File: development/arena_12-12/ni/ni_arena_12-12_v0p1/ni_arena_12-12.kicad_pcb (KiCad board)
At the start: 6 copper layers, 228.6 x 228.6 mm, 581 parts, among them J1 Barrel_Jack, J2 NI_TE_68pos, J3 Barrel_Jack, P1 CONN15, P10 CONN15, P11 CONN15, P12 CONN15, P2 CONN15, P3 CONN15, P4 CONN15, P5 CONN15, P6 CONN15, P7 CONN15, P8 CONN15, P9 CONN15, Q1 MOSFET_NCHAN, SW1 SW_SPDT, U1 AP2112K-3.3, U10 TXB0108PW, U100 74LVC2G17, U101 74LVC2G17, U102 74LVC2G17, U103 74LVC2G17, U104 74LVC2G17, U105 74LVC2G17, U106 74LVC2G17, U107 74LVC2G17, U108 74LVC2G17, U109 74LVC2G17, U11 TXB0108PW, U110 74LVC2G17, U12 TXB0108PW, U13 TXB0108PW, U14 TXB0108PW, U15 TXB0108PW, U16 TXB0108PW, U17 TXB0108PW, U18 TXB0108PW, U19 74LVC2G17, U2 TXB0108PW, U20 74LVC2G17, U21 74LVC2G17, U22 74LVC2G17, U23 74LVC2G17, U24 74LVC2G17, U25 74LVC2G17, U26 74LVC2G17, U27 74LVC2G17, U28 74LVC2G17, U29 74LVC2G17, U3 TXB0108PW, U30 74LVC2G17, U31 74LVC2G17, U32 74LVC2G17, U33 74LVC2G17, U34 74LVC2G17, U35 74LVC2G17, U36 74LVC2G17, U37 74LVC2G17, U38 74LVC2G17, U39 74LVC2G17, U4 TXB0108PW, U40 74LVC2G17, U41 74LVC2G17, U42 74LVC2G17, U43 74LVC2G17, U44 74LVC2G17, U45 74LVC2G17, U46 74LVC2G17, U47 74LVC2G17, U48 74LVC2G17, U49 74LVC2G17, U5 TXB0108PW, U50 74LVC2G17, U51 74LVC2G17, U52 74LVC2G17, U53 74LVC2G17, U54 74LVC2G17, U55 74LVC2G17, U56 74LVC2G17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

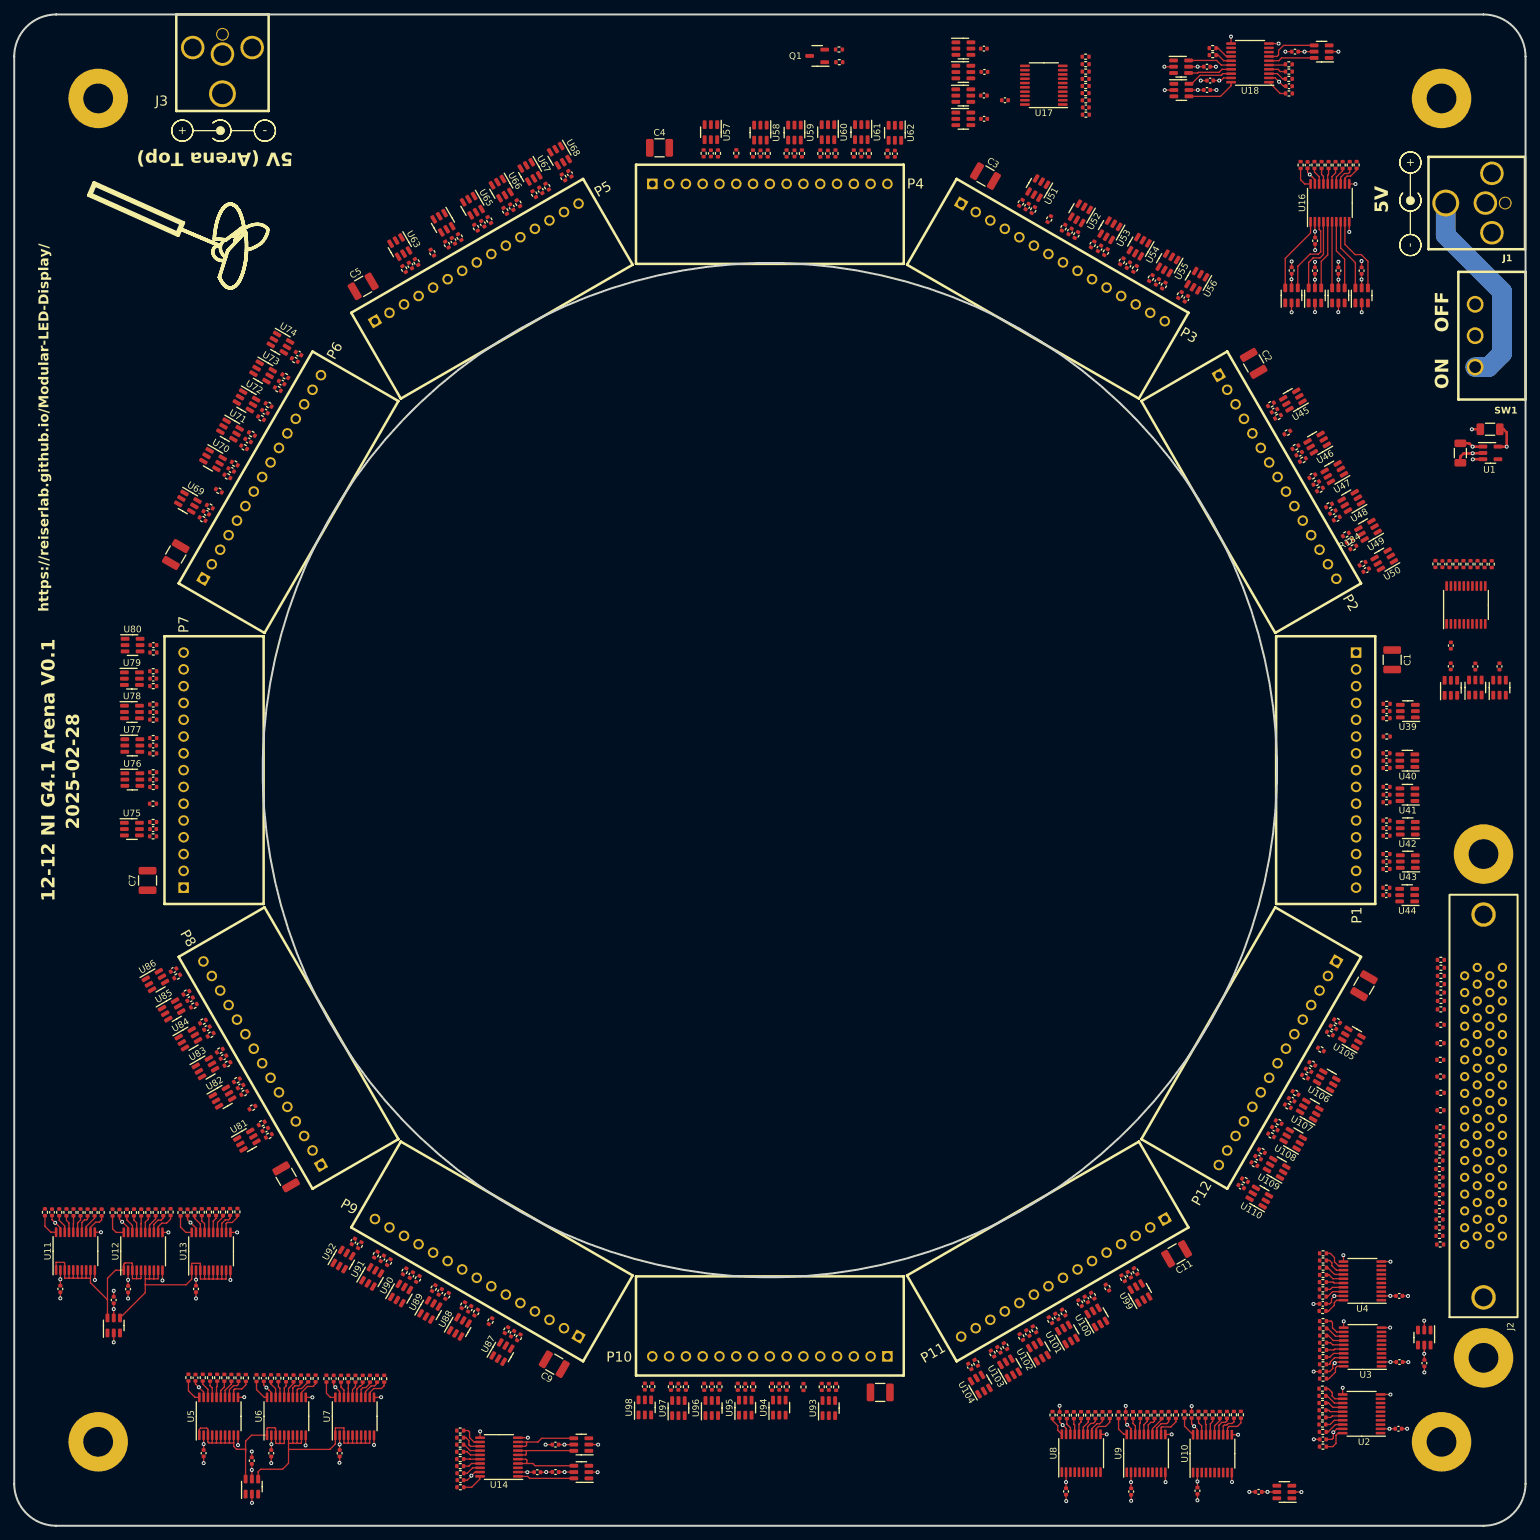
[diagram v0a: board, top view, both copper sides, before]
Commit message: Worked on routing 12-12 NI arena.
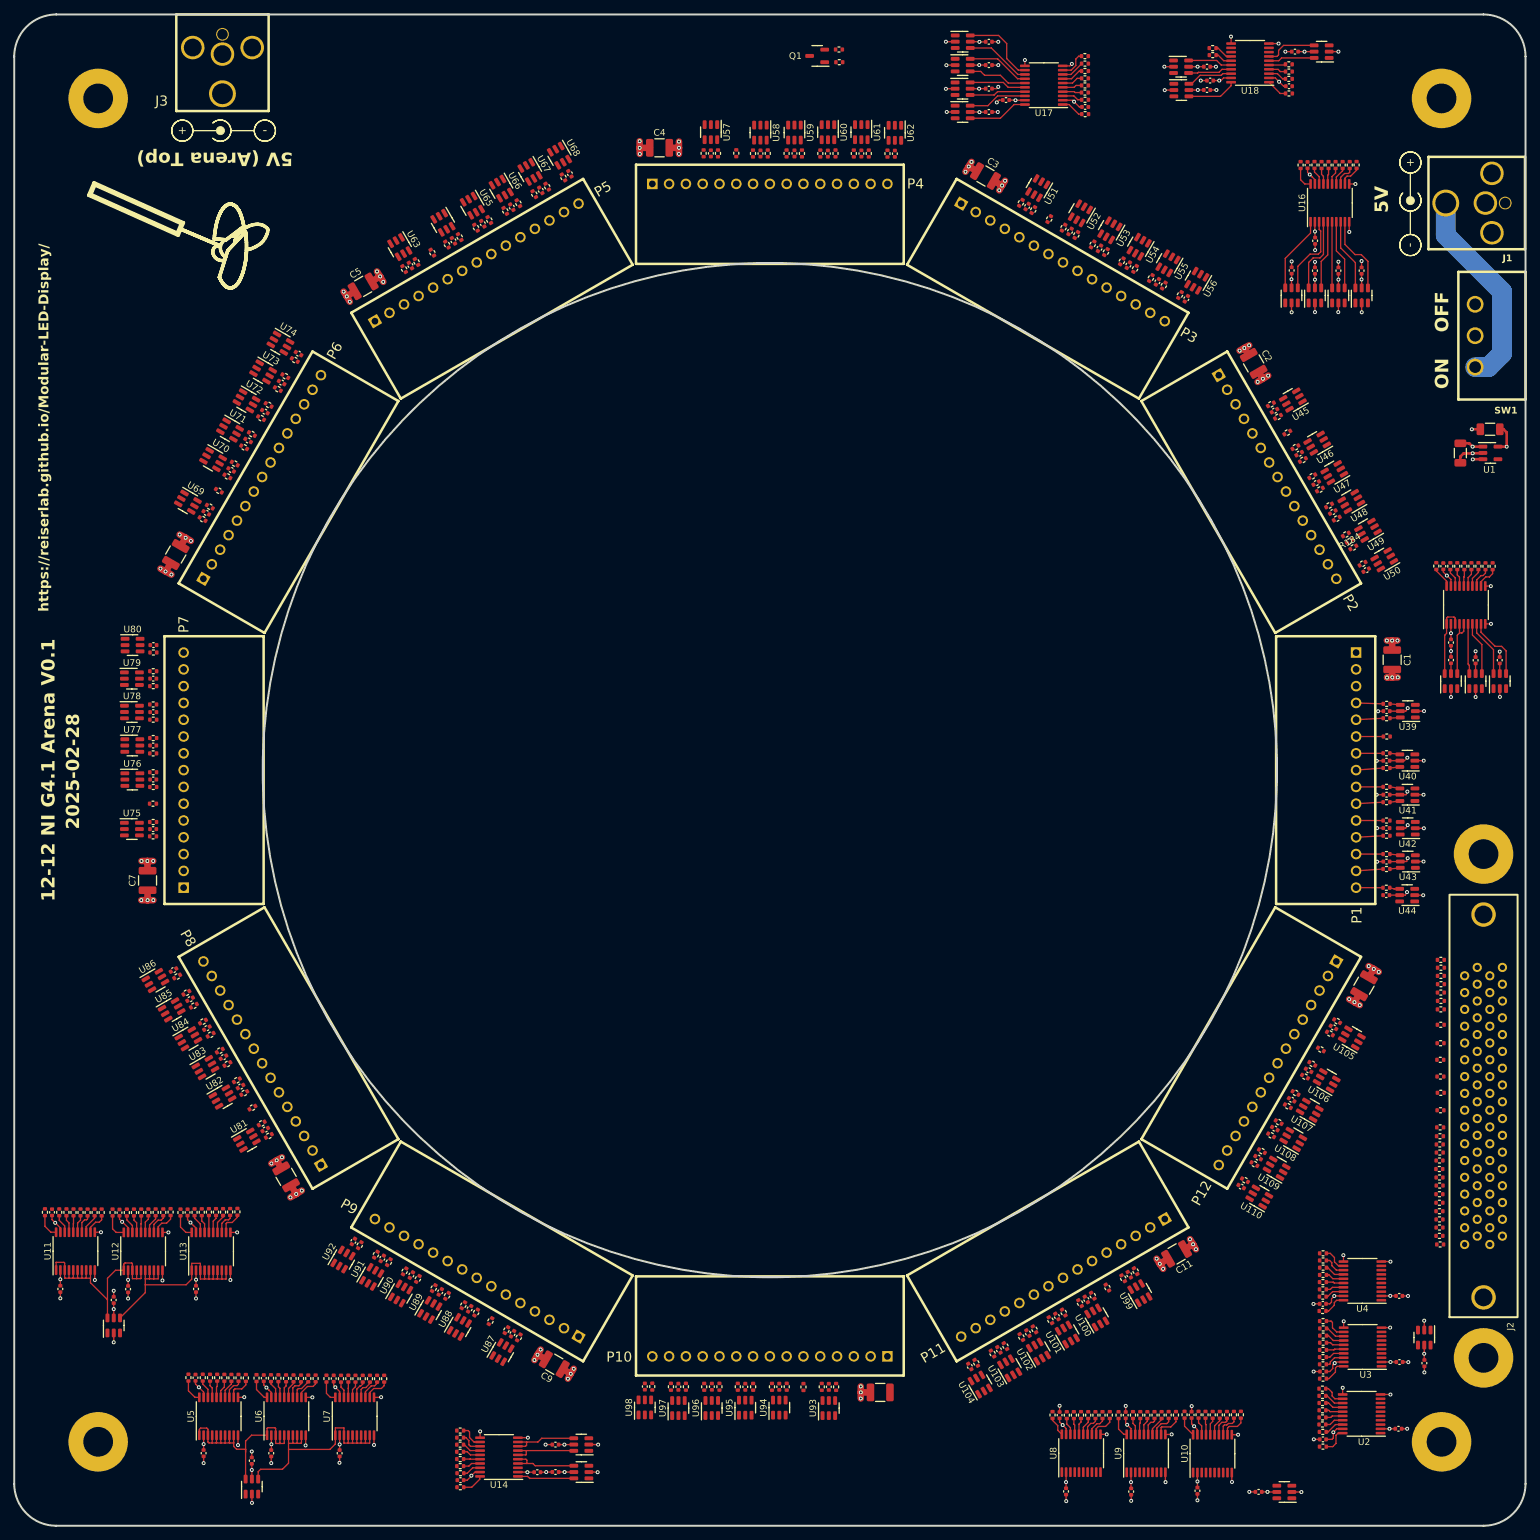
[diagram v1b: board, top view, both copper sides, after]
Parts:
- moved C30 1.28 mm to (210.9, 74.7)
- moved C31 1.28 mm to (210.9, 67.6)
- moved C28 1.26 mm to (210.9, 78.2)
- moved C29 1.23 mm to (210.9, 71.2)
- moved U30 1.06 mm to (207.0, 71.2)
- moved U28 1.05 mm to (207.0, 78.2)
- moved U29 1.05 mm to (207.0, 74.7)
- moved U31 1.05 mm to (207.0, 67.6)
- moved U25 1.02 mm to (280.8, 164.3)
- moved U27 0.99 mm to (288.2, 164.3)
- moved U26 0.97 mm to (284.6, 164.3)
- moved C22 0.95 mm to (284.6, 161.2)
- moved C21 0.95 mm to (280.8, 161.2)
- moved C23 0.95 mm to (288.2, 161.2)
- moved C133 0.46 mm to (280.8, 158.5)
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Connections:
- U31 pad 4: Net-(U17-B8) -> Net-(U17-B7)
- U31 pad 6: Net-(U17-B7) -> Net-(U17-B8)
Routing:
- net GND: track 71.6 -> 142.0 mm, vias 63 -> 127
- net +5V: track 55.4 -> 122.0 mm, vias 19 -> 64
- net +3.3V: track 85.8 -> 98.5 mm, vias 41 -> 45
- net Net-(U17-B8): track 0.00 -> 11.8 mm
- net Net-(U15-A1): track 0.00 -> 10.8 mm
- net Net-(U17-B7): track 0.00 -> 9.92 mm
- net Net-(U15-A8): track 0.00 -> 9.66 mm
- net Net-(U17-B6): track 0.00 -> 9.53 mm
- net Net-(U15-A3): track 0.00 -> 9.52 mm
- net Net-(U17-B1): track 0.00 -> 9.14 mm
- net Net-(U17-B5): track 0.00 -> 9.01 mm
- net Net-(U17-B2): track 0.00 -> 8.89 mm
- net Net-(U17-B4): track 0.00 -> 8.59 mm
- net Net-(U15-A7): track 0.00 -> 8.57 mm
- net Net-(U17-B3): track 0.00 -> 8.49 mm
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
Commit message: Finished preliminary hand routing for NI 12-12 arena.
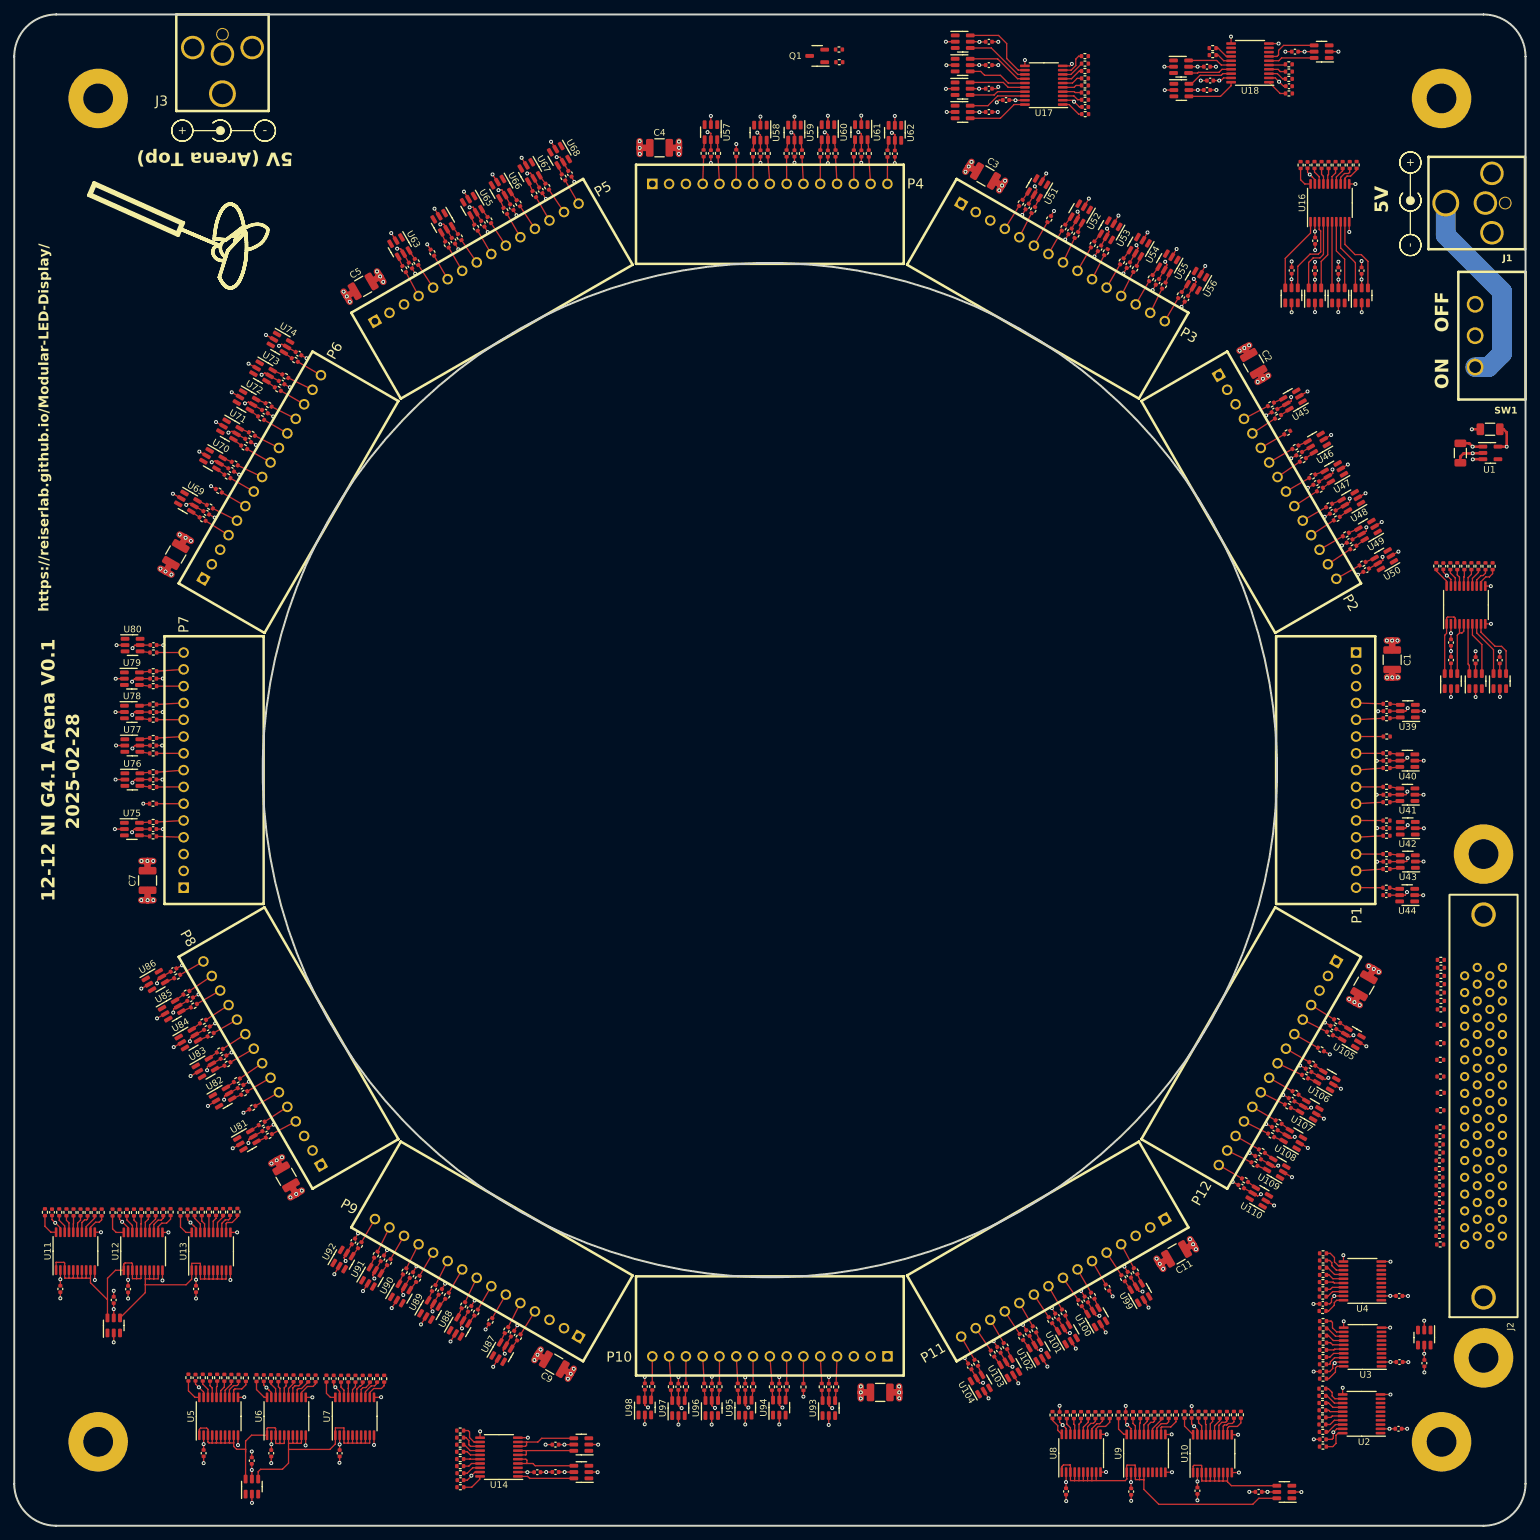
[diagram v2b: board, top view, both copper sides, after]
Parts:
- turned R177 to -150 degrees
- turned R180 to -150 degrees
- turned R189 to -120 degrees
- turned R192 to -120 degrees
- turned R201 to -90 degrees
- turned R204 to -90 degrees
- turned R213 to -60 degrees
- turned R216 to -60 degrees
- turned R225 to -30 degrees
- turned R228 to -30 degrees
- turned R237 to 0 degrees
- turned R240 to 0 degrees
- turned R249 to 30 degrees
- turned R252 to 30 degrees
- turned R261 to 60 degrees
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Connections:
- U100 pad 1: /Level Shifters/PAN5V.CS_0_P11 -> /Level Shifters/PAN5V.CS_1_P11
- U100 pad 3: /Level Shifters/PAN5V.CS_1_P11 -> /Level Shifters/PAN5V.CS_0_P11
- U100 pad 4: Net-(R287-Pad1) -> Net-(R286-Pad1)
- U100 pad 6: Net-(R286-Pad1) -> Net-(R287-Pad1)
- U101 pad 1: /Level Shifters/PAN5V.CS_2_P11 -> /Level Shifters/PAN5V.CS_3_P11
- U101 pad 3: /Level Shifters/PAN5V.CS_3_P11 -> /Level Shifters/PAN5V.CS_2_P11
- U101 pad 4: Net-(R289-Pad1) -> Net-(R288-Pad1)
- U101 pad 6: Net-(R288-Pad1) -> Net-(R289-Pad1)
- U102 pad 1: /Level Shifters/PAN5V.CS_4_P11 -> /Level Shifters/PAN5V.CS_5_P11
- U102 pad 3: /Level Shifters/PAN5V.CS_5_P11 -> /Level Shifters/PAN5V.CS_4_P11
- U102 pad 4: Net-(R291-Pad1) -> Net-(R290-Pad1)
- U102 pad 6: Net-(R290-Pad1) -> Net-(R291-Pad1)
- U103 pad 1: /Level Shifters/PAN5V.CS_6_P11 -> /Level Shifters/PAN5V.CS_7_P11
- U103 pad 3: /Level Shifters/PAN5V.CS_7_P11 -> /Level Shifters/PAN5V.CS_6_P11
- U103 pad 4: Net-(R293-Pad1) -> Net-(R292-Pad1)
- U103 pad 6: Net-(R292-Pad1) -> Net-(R293-Pad1)
- U104 pad 1: /Level Shifters/PAN5V.EXT_INT -> unconnected-(U104-Pad1)
- U104 pad 3: unconnected-(U104-Pad3) -> /Level Shifters/PAN5V.EXT_INT
- U104 pad 4: unconnected-(U104-Pad4) -> Net-(R294-Pad1)
- U104 pad 6: Net-(R294-Pad1) -> unconnected-(U104-Pad6)
- U105 pad 1: /Level Shifters/PAN5V.SCK_5_H2 -> /Level Shifters/PAN5V.MOSI_11
- U105 pad 3: /Level Shifters/PAN5V.MOSI_11 -> /Level Shifters/PAN5V.SCK_5_H2
- U105 pad 4: Net-(R296-Pad1) -> Net-(R295-Pad1)
- U105 pad 6: Net-(R295-Pad1) -> Net-(R296-Pad1)
- U106 pad 1: /Level Shifters/PAN5V.CS_0_P12 -> /Level Shifters/PAN5V.CS_1_P12
- U106 pad 3: /Level Shifters/PAN5V.CS_1_P12 -> /Level Shifters/PAN5V.CS_0_P12
- U106 pad 4: Net-(R299-Pad1) -> Net-(R298-Pad1)
- U106 pad 6: Net-(R298-Pad1) -> Net-(R299-Pad1)
- U107 pad 1: /Level Shifters/PAN5V.CS_2_P12 -> /Level Shifters/PAN5V.CS_3_P12
- U107 pad 3: /Level Shifters/PAN5V.CS_3_P12 -> /Level Shifters/PAN5V.CS_2_P12
- U107 pad 4: Net-(R301-Pad1) -> Net-(R300-Pad1)
- U107 pad 6: Net-(R300-Pad1) -> Net-(R301-Pad1)
- U108 pad 1: /Level Shifters/PAN5V.CS_4_P12 -> /Level Shifters/PAN5V.CS_5_P12
- U108 pad 3: /Level Shifters/PAN5V.CS_5_P12 -> /Level Shifters/PAN5V.CS_4_P12
- U108 pad 4: Net-(R303-Pad1) -> Net-(R302-Pad1)
- U108 pad 6: Net-(R302-Pad1) -> Net-(R303-Pad1)
- U109 pad 1: /Level Shifters/PAN5V.CS_6_P12 -> /Level Shifters/PAN5V.CS_7_P12
- U109 pad 3: /Level Shifters/PAN5V.CS_7_P12 -> /Level Shifters/PAN5V.CS_6_P12
- U109 pad 4: Net-(R305-Pad1) -> Net-(R304-Pad1)
- U109 pad 6: Net-(R304-Pad1) -> Net-(R305-Pad1)
- U110 pad 1: /Level Shifters/PAN5V.EXT_INT -> unconnected-(U110-Pad1)
- U110 pad 3: unconnected-(U110-Pad3) -> /Level Shifters/PAN5V.EXT_INT
- U110 pad 4: unconnected-(U110-Pad4) -> Net-(R306-Pad1)
- U110 pad 6: Net-(R306-Pad1) -> unconnected-(U110-Pad6)
- U45 pad 1: /Level Shifters/PAN5V.SCK_1_H1 -> /Level Shifters/PAN5V.MOSI_01
- U45 pad 3: /Level Shifters/PAN5V.MOSI_01 -> /Level Shifters/PAN5V.SCK_1_H1
- U45 pad 4: Net-(R176-Pad1) -> Net-(R175-Pad1)
- U45 pad 6: Net-(R175-Pad1) -> Net-(R176-Pad1)
- U46 pad 1: /Level Shifters/PAN5V.CS_0_P02 -> /Level Shifters/PAN5V.CS_1_P02
- U46 pad 3: /Level Shifters/PAN5V.CS_1_P02 -> /Level Shifters/PAN5V.CS_0_P02
- U46 pad 4: Net-(R179-Pad1) -> Net-(R178-Pad1)
- U46 pad 6: Net-(R178-Pad1) -> Net-(R179-Pad1)
- U47 pad 1: /Level Shifters/PAN5V.CS_2_P02 -> /Level Shifters/PAN5V.CS_3_P02
- U47 pad 3: /Level Shifters/PAN5V.CS_3_P02 -> /Level Shifters/PAN5V.CS_2_P02
- U47 pad 4: Net-(R181-Pad1) -> Net-(R180-Pad1)
- U47 pad 6: Net-(R180-Pad1) -> Net-(R181-Pad1)
- U48 pad 1: /Level Shifters/PAN5V.CS_4_P02 -> /Level Shifters/PAN5V.CS_5_P02
- U48 pad 3: /Level Shifters/PAN5V.CS_5_P02 -> /Level Shifters/PAN5V.CS_4_P02
- U48 pad 4: Net-(R183-Pad1) -> Net-(R182-Pad1)
- U48 pad 6: Net-(R182-Pad1) -> Net-(R183-Pad1)
- U49 pad 1: /Level Shifters/PAN5V.CS_6_P02 -> /Level Shifters/PAN5V.CS_7_P02
- U49 pad 3: /Level Shifters/PAN5V.CS_7_P02 -> /Level Shifters/PAN5V.CS_6_P02
- U49 pad 4: Net-(R185-Pad1) -> Net-(R184-Pad1)
- U49 pad 6: Net-(R184-Pad1) -> Net-(R185-Pad1)
- U50 pad 1: /Level Shifters/PAN5V.EXT_INT -> unconnected-(U50-Pad1)
- U50 pad 3: unconnected-(U50-Pad3) -> /Level Shifters/PAN5V.EXT_INT
- U50 pad 4: unconnected-(U50-Pad4) -> Net-(R186-Pad1)
- U50 pad 6: Net-(R186-Pad1) -> unconnected-(U50-Pad6)
- U51 pad 1: /Level Shifters/PAN5V.SCK_2_H1 -> /Level Shifters/PAN5V.MOSI_02
- U51 pad 3: /Level Shifters/PAN5V.MOSI_02 -> /Level Shifters/PAN5V.SCK_2_H1
- U51 pad 4: Net-(R188-Pad1) -> Net-(R187-Pad1)
- U51 pad 6: Net-(R187-Pad1) -> Net-(R188-Pad1)
- U52 pad 1: /Level Shifters/PAN5V.CS_0_P03 -> /Level Shifters/PAN5V.CS_1_P03
- U52 pad 3: /Level Shifters/PAN5V.CS_1_P03 -> /Level Shifters/PAN5V.CS_0_P03
- U52 pad 4: Net-(R191-Pad1) -> Net-(R190-Pad1)
- U52 pad 6: Net-(R190-Pad1) -> Net-(R191-Pad1)
- U53 pad 1: /Level Shifters/PAN5V.CS_2_P03 -> /Level Shifters/PAN5V.CS_3_P03
- U53 pad 3: /Level Shifters/PAN5V.CS_3_P03 -> /Level Shifters/PAN5V.CS_2_P03
- U53 pad 4: Net-(R193-Pad1) -> Net-(R192-Pad1)
- U53 pad 6: Net-(R192-Pad1) -> Net-(R193-Pad1)
- U54 pad 1: /Level Shifters/PAN5V.CS_4_P03 -> /Level Shifters/PAN5V.CS_5_P03
- U54 pad 3: /Level Shifters/PAN5V.CS_5_P03 -> /Level Shifters/PAN5V.CS_4_P03
- U54 pad 4: Net-(R195-Pad1) -> Net-(R194-Pad1)
- U54 pad 6: Net-(R194-Pad1) -> Net-(R195-Pad1)
- U55 pad 1: /Level Shifters/PAN5V.CS_6_P03 -> /Level Shifters/PAN5V.CS_7_P03
- U55 pad 3: /Level Shifters/PAN5V.CS_7_P03 -> /Level Shifters/PAN5V.CS_6_P03
- U55 pad 4: Net-(R197-Pad1) -> Net-(R196-Pad1)
- U55 pad 6: Net-(R196-Pad1) -> Net-(R197-Pad1)
- U56 pad 1: /Level Shifters/PAN5V.EXT_INT -> unconnected-(U56-Pad1)
- U56 pad 3: unconnected-(U56-Pad3) -> /Level Shifters/PAN5V.EXT_INT
- U56 pad 4: unconnected-(U56-Pad4) -> Net-(R198-Pad1)
- U56 pad 6: Net-(R198-Pad1) -> unconnected-(U56-Pad6)
- U57 pad 1: /Level Shifters/PAN5V.SCK_3_H1 -> /Level Shifters/PAN5V.MOSI_03
- U57 pad 3: /Level Shifters/PAN5V.MOSI_03 -> /Level Shifters/PAN5V.SCK_3_H1
- U57 pad 4: Net-(R200-Pad1) -> Net-(R199-Pad1)
- U57 pad 6: Net-(R199-Pad1) -> Net-(R200-Pad1)
- U58 pad 1: /Level Shifters/PAN5V.CS_0_P04 -> /Level Shifters/PAN5V.CS_1_P04
- U58 pad 3: /Level Shifters/PAN5V.CS_1_P04 -> /Level Shifters/PAN5V.CS_0_P04
- U58 pad 4: Net-(R203-Pad1) -> Net-(R202-Pad1)
- U58 pad 6: Net-(R202-Pad1) -> Net-(R203-Pad1)
- U59 pad 1: /Level Shifters/PAN5V.CS_2_P04 -> /Level Shifters/PAN5V.CS_3_P04
- U59 pad 3: /Level Shifters/PAN5V.CS_3_P04 -> /Level Shifters/PAN5V.CS_2_P04
- U59 pad 4: Net-(R205-Pad1) -> Net-(R204-Pad1)
- U59 pad 6: Net-(R204-Pad1) -> Net-(R205-Pad1)
- U60 pad 1: /Level Shifters/PAN5V.CS_4_P04 -> /Level Shifters/PAN5V.CS_5_P04
- U60 pad 3: /Level Shifters/PAN5V.CS_5_P04 -> /Level Shifters/PAN5V.CS_4_P04
- U60 pad 4: Net-(R207-Pad1) -> Net-(R206-Pad1)
- U60 pad 6: Net-(R206-Pad1) -> Net-(R207-Pad1)
- U61 pad 1: /Level Shifters/PAN5V.CS_6_P04 -> /Level Shifters/PAN5V.CS_7_P04
- U61 pad 3: /Level Shifters/PAN5V.CS_7_P04 -> /Level Shifters/PAN5V.CS_6_P04
- U61 pad 4: Net-(R209-Pad1) -> Net-(R208-Pad1)
- U61 pad 6: Net-(R208-Pad1) -> Net-(R209-Pad1)
- U62 pad 1: /Level Shifters/PAN5V.EXT_INT -> unconnected-(U62-Pad1)
- U62 pad 3: unconnected-(U62-Pad3) -> /Level Shifters/PAN5V.EXT_INT
- U62 pad 4: unconnected-(U62-Pad4) -> Net-(R210-Pad1)
- U62 pad 6: Net-(R210-Pad1) -> unconnected-(U62-Pad6)
- U63 pad 1: /Level Shifters/PAN5V.SCK_4_H1 -> /Level Shifters/PAN5V.MOSI_04
- U63 pad 3: /Level Shifters/PAN5V.MOSI_04 -> /Level Shifters/PAN5V.SCK_4_H1
- U63 pad 4: Net-(R212-Pad1) -> Net-(R211-Pad1)
- U63 pad 6: Net-(R211-Pad1) -> Net-(R212-Pad1)
- U64 pad 1: /Level Shifters/PAN5V.CS_0_P05 -> /Level Shifters/PAN5V.CS_1_P05
- U64 pad 3: /Level Shifters/PAN5V.CS_1_P05 -> /Level Shifters/PAN5V.CS_0_P05
- U64 pad 4: Net-(R215-Pad1) -> Net-(R214-Pad1)
- U64 pad 6: Net-(R214-Pad1) -> Net-(R215-Pad1)
- U65 pad 1: /Level Shifters/PAN5V.CS_2_P05 -> /Level Shifters/PAN5V.CS_3_P05
- U65 pad 3: /Level Shifters/PAN5V.CS_3_P05 -> /Level Shifters/PAN5V.CS_2_P05
- U65 pad 4: Net-(R217-Pad1) -> Net-(R216-Pad1)
- U65 pad 6: Net-(R216-Pad1) -> Net-(R217-Pad1)
- U66 pad 1: /Level Shifters/PAN5V.CS_4_P05 -> /Level Shifters/PAN5V.CS_5_P05
- U66 pad 3: /Level Shifters/PAN5V.CS_5_P05 -> /Level Shifters/PAN5V.CS_4_P05
- U66 pad 4: Net-(R219-Pad1) -> Net-(R218-Pad1)
- U66 pad 6: Net-(R218-Pad1) -> Net-(R219-Pad1)
- U67 pad 1: /Level Shifters/PAN5V.CS_6_P05 -> /Level Shifters/PAN5V.CS_7_P05
- U67 pad 3: /Level Shifters/PAN5V.CS_7_P05 -> /Level Shifters/PAN5V.CS_6_P05
- U67 pad 4: Net-(R221-Pad1) -> Net-(R220-Pad1)
- U67 pad 6: Net-(R220-Pad1) -> Net-(R221-Pad1)
- U68 pad 1: /Level Shifters/PAN5V.EXT_INT -> unconnected-(U68-Pad1)
- U68 pad 3: unconnected-(U68-Pad3) -> /Level Shifters/PAN5V.EXT_INT
- U68 pad 4: unconnected-(U68-Pad4) -> Net-(R222-Pad1)
- U68 pad 6: Net-(R222-Pad1) -> unconnected-(U68-Pad6)
- U69 pad 1: /Level Shifters/PAN5V.SCK_5_H1 -> /Level Shifters/PAN5V.MOSI_05
- U69 pad 3: /Level Shifters/PAN5V.MOSI_05 -> /Level Shifters/PAN5V.SCK_5_H1
- U69 pad 4: Net-(R224-Pad1) -> Net-(R223-Pad1)
- U69 pad 6: Net-(R223-Pad1) -> Net-(R224-Pad1)
- U70 pad 1: /Level Shifters/PAN5V.CS_0_P06 -> /Level Shifters/PAN5V.CS_1_P06
- U70 pad 3: /Level Shifters/PAN5V.CS_1_P06 -> /Level Shifters/PAN5V.CS_0_P06
- U70 pad 4: Net-(R227-Pad1) -> Net-(R226-Pad1)
- U70 pad 6: Net-(R226-Pad1) -> Net-(R227-Pad1)
- U71 pad 1: /Level Shifters/PAN5V.CS_2_P06 -> /Level Shifters/PAN5V.CS_3_P06
- U71 pad 3: /Level Shifters/PAN5V.CS_3_P06 -> /Level Shifters/PAN5V.CS_2_P06
- U71 pad 4: Net-(R229-Pad1) -> Net-(R228-Pad1)
- U71 pad 6: Net-(R228-Pad1) -> Net-(R229-Pad1)
- U72 pad 1: /Level Shifters/PAN5V.CS_4_P06 -> /Level Shifters/PAN5V.CS_5_P06
- U72 pad 3: /Level Shifters/PAN5V.CS_5_P06 -> /Level Shifters/PAN5V.CS_4_P06
- U72 pad 4: Net-(R231-Pad1) -> Net-(R230-Pad1)
- U72 pad 6: Net-(R230-Pad1) -> Net-(R231-Pad1)
- U73 pad 1: /Level Shifters/PAN5V.CS_6_P06 -> /Level Shifters/PAN5V.CS_7_P06
- U73 pad 3: /Level Shifters/PAN5V.CS_7_P06 -> /Level Shifters/PAN5V.CS_6_P06
- U73 pad 4: Net-(R233-Pad1) -> Net-(R232-Pad1)
- U73 pad 6: Net-(R232-Pad1) -> Net-(R233-Pad1)
- U74 pad 1: /Level Shifters/PAN5V.EXT_INT -> unconnected-(U74-Pad1)
- U74 pad 3: unconnected-(U74-Pad3) -> /Level Shifters/PAN5V.EXT_INT
- U74 pad 4: unconnected-(U74-Pad4) -> Net-(R234-Pad1)
- U74 pad 6: Net-(R234-Pad1) -> unconnected-(U74-Pad6)
- U75 pad 1: /Level Shifters/PAN5V.SCK_0_H2 -> /Level Shifters/PAN5V.MOSI_06
- U75 pad 3: /Level Shifters/PAN5V.MOSI_06 -> /Level Shifters/PAN5V.SCK_0_H2
- U75 pad 4: Net-(R236-Pad1) -> Net-(R235-Pad1)
- U75 pad 6: Net-(R235-Pad1) -> Net-(R236-Pad1)
- U76 pad 1: /Level Shifters/PAN5V.CS_0_P07 -> /Level Shifters/PAN5V.CS_1_P07
- U76 pad 3: /Level Shifters/PAN5V.CS_1_P07 -> /Level Shifters/PAN5V.CS_0_P07
- U76 pad 4: Net-(R239-Pad1) -> Net-(R238-Pad1)
- U76 pad 6: Net-(R238-Pad1) -> Net-(R239-Pad1)
- U77 pad 1: /Level Shifters/PAN5V.CS_2_P07 -> /Level Shifters/PAN5V.CS_3_P07
- U77 pad 3: /Level Shifters/PAN5V.CS_3_P07 -> /Level Shifters/PAN5V.CS_2_P07
- U77 pad 4: Net-(R241-Pad1) -> Net-(R240-Pad1)
- U77 pad 6: Net-(R240-Pad1) -> Net-(R241-Pad1)
- U78 pad 1: /Level Shifters/PAN5V.CS_4_P07 -> /Level Shifters/PAN5V.CS_5_P07
- U78 pad 3: /Level Shifters/PAN5V.CS_5_P07 -> /Level Shifters/PAN5V.CS_4_P07
- U78 pad 4: Net-(R243-Pad1) -> Net-(R242-Pad1)
- U78 pad 6: Net-(R242-Pad1) -> Net-(R243-Pad1)
- U79 pad 1: /Level Shifters/PAN5V.CS_6_P07 -> /Level Shifters/PAN5V.CS_7_P07
- U79 pad 3: /Level Shifters/PAN5V.CS_7_P07 -> /Level Shifters/PAN5V.CS_6_P07
- U79 pad 4: Net-(R245-Pad1) -> Net-(R244-Pad1)
- U79 pad 6: Net-(R244-Pad1) -> Net-(R245-Pad1)
- U80 pad 1: /Level Shifters/PAN5V.EXT_INT -> unconnected-(U80-Pad1)
- U80 pad 3: unconnected-(U80-Pad3) -> /Level Shifters/PAN5V.EXT_INT
- U80 pad 4: unconnected-(U80-Pad4) -> Net-(R246-Pad1)
- U80 pad 6: Net-(R246-Pad1) -> unconnected-(U80-Pad6)
- U81 pad 1: /Level Shifters/PAN5V.SCK_1_H2 -> /Level Shifters/PAN5V.MOSI_07
- U81 pad 3: /Level Shifters/PAN5V.MOSI_07 -> /Level Shifters/PAN5V.SCK_1_H2
- U81 pad 4: Net-(R248-Pad1) -> Net-(R247-Pad1)
- U81 pad 6: Net-(R247-Pad1) -> Net-(R248-Pad1)
- U82 pad 1: /Level Shifters/PAN5V.CS_0_P08 -> /Level Shifters/PAN5V.CS_1_P08
- U82 pad 3: /Level Shifters/PAN5V.CS_1_P08 -> /Level Shifters/PAN5V.CS_0_P08
- U82 pad 4: Net-(R251-Pad1) -> Net-(R250-Pad1)
- U82 pad 6: Net-(R250-Pad1) -> Net-(R251-Pad1)
- U83 pad 1: /Level Shifters/PAN5V.CS_2_P08 -> /Level Shifters/PAN5V.CS_3_P08
- U83 pad 3: /Level Shifters/PAN5V.CS_3_P08 -> /Level Shifters/PAN5V.CS_2_P08
- U83 pad 4: Net-(R253-Pad1) -> Net-(R252-Pad1)
- U83 pad 6: Net-(R252-Pad1) -> Net-(R253-Pad1)
- U84 pad 1: /Level Shifters/PAN5V.CS_4_P08 -> /Level Shifters/PAN5V.CS_5_P08
- U84 pad 3: /Level Shifters/PAN5V.CS_5_P08 -> /Level Shifters/PAN5V.CS_4_P08
- U84 pad 4: Net-(R255-Pad1) -> Net-(R254-Pad1)
- U84 pad 6: Net-(R254-Pad1) -> Net-(R255-Pad1)
- U85 pad 1: /Level Shifters/PAN5V.CS_6_P08 -> /Level Shifters/PAN5V.CS_7_P08
- U85 pad 3: /Level Shifters/PAN5V.CS_7_P08 -> /Level Shifters/PAN5V.CS_6_P08
- U85 pad 4: Net-(R257-Pad1) -> Net-(R256-Pad1)
- U85 pad 6: Net-(R256-Pad1) -> Net-(R257-Pad1)
- U86 pad 1: /Level Shifters/PAN5V.EXT_INT -> unconnected-(U86-Pad1)
- U86 pad 3: unconnected-(U86-Pad3) -> /Level Shifters/PAN5V.EXT_INT
- U86 pad 4: unconnected-(U86-Pad4) -> Net-(R258-Pad1)
- U86 pad 6: Net-(R258-Pad1) -> unconnected-(U86-Pad6)
- U87 pad 1: /Level Shifters/PAN5V.SCK_2_H2 -> /Level Shifters/PAN5V.MOSI_08
- U87 pad 3: /Level Shifters/PAN5V.MOSI_08 -> /Level Shifters/PAN5V.SCK_2_H2
- U87 pad 4: Net-(R260-Pad1) -> Net-(R259-Pad1)
- U87 pad 6: Net-(R259-Pad1) -> Net-(R260-Pad1)
- U88 pad 1: /Level Shifters/PAN5V.CS_0_P09 -> /Level Shifters/PAN5V.CS_1_P09
- U88 pad 3: /Level Shifters/PAN5V.CS_1_P09 -> /Level Shifters/PAN5V.CS_0_P09
- U88 pad 4: Net-(R263-Pad1) -> Net-(R262-Pad1)
- U88 pad 6: Net-(R262-Pad1) -> Net-(R263-Pad1)
- U89 pad 1: /Level Shifters/PAN5V.CS_2_P09 -> /Level Shifters/PAN5V.CS_3_P09
- U89 pad 3: /Level Shifters/PAN5V.CS_3_P09 -> /Level Shifters/PAN5V.CS_2_P09
- U89 pad 4: Net-(R265-Pad1) -> Net-(R264-Pad1)
- U89 pad 6: Net-(R264-Pad1) -> Net-(R265-Pad1)
- U90 pad 1: /Level Shifters/PAN5V.CS_4_P09 -> /Level Shifters/PAN5V.CS_5_P09
- U90 pad 3: /Level Shifters/PAN5V.CS_5_P09 -> /Level Shifters/PAN5V.CS_4_P09
- U90 pad 4: Net-(R267-Pad1) -> Net-(R266-Pad1)
- U90 pad 6: Net-(R266-Pad1) -> Net-(R267-Pad1)
- U91 pad 1: /Level Shifters/PAN5V.CS_6_P09 -> /Level Shifters/PAN5V.CS_7_P09
- U91 pad 3: /Level Shifters/PAN5V.CS_7_P09 -> /Level Shifters/PAN5V.CS_6_P09
- U91 pad 4: Net-(R269-Pad1) -> Net-(R268-Pad1)
- U91 pad 6: Net-(R268-Pad1) -> Net-(R269-Pad1)
- U92 pad 1: /Level Shifters/PAN5V.EXT_INT -> unconnected-(U92-Pad1)
- U92 pad 3: unconnected-(U92-Pad3) -> /Level Shifters/PAN5V.EXT_INT
- U92 pad 4: unconnected-(U92-Pad4) -> Net-(R270-Pad1)
- U92 pad 6: Net-(R270-Pad1) -> unconnected-(U92-Pad6)
- U93 pad 1: /Level Shifters/PAN5V.SCK_3_H2 -> /Level Shifters/PAN5V.MOSI_09
- U93 pad 3: /Level Shifters/PAN5V.MOSI_09 -> /Level Shifters/PAN5V.SCK_3_H2
- U93 pad 4: Net-(R272-Pad1) -> Net-(R271-Pad1)
- U93 pad 6: Net-(R271-Pad1) -> Net-(R272-Pad1)
- U94 pad 1: /Level Shifters/PAN5V.CS_0_P10 -> /Level Shifters/PAN5V.CS_1_P10
- U94 pad 3: /Level Shifters/PAN5V.CS_1_P10 -> /Level Shifters/PAN5V.CS_0_P10
- U94 pad 4: Net-(R275-Pad1) -> Net-(R274-Pad1)
- U94 pad 6: Net-(R274-Pad1) -> Net-(R275-Pad1)
- U95 pad 1: /Level Shifters/PAN5V.CS_2_P10 -> /Level Shifters/PAN5V.CS_3_P10
- U95 pad 3: /Level Shifters/PAN5V.CS_3_P10 -> /Level Shifters/PAN5V.CS_2_P10
- U95 pad 4: Net-(R277-Pad1) -> Net-(R276-Pad1)
- U95 pad 6: Net-(R276-Pad1) -> Net-(R277-Pad1)
- U96 pad 1: /Level Shifters/PAN5V.CS_4_P10 -> /Level Shifters/PAN5V.CS_5_P10
- U96 pad 3: /Level Shifters/PAN5V.CS_5_P10 -> /Level Shifters/PAN5V.CS_4_P10
- U96 pad 4: Net-(R279-Pad1) -> Net-(R278-Pad1)
- U96 pad 6: Net-(R278-Pad1) -> Net-(R279-Pad1)
- U97 pad 1: /Level Shifters/PAN5V.CS_6_P10 -> /Level Shifters/PAN5V.CS_7_P10
- U97 pad 3: /Level Shifters/PAN5V.CS_7_P10 -> /Level Shifters/PAN5V.CS_6_P10
- U97 pad 4: Net-(R281-Pad1) -> Net-(R280-Pad1)
- U97 pad 6: Net-(R280-Pad1) -> Net-(R281-Pad1)
- U98 pad 1: /Level Shifters/PAN5V.EXT_INT -> unconnected-(U98-Pad1)
- U98 pad 3: unconnected-(U98-Pad3) -> /Level Shifters/PAN5V.EXT_INT
- U98 pad 4: unconnected-(U98-Pad4) -> Net-(R282-Pad1)
- U98 pad 6: Net-(R282-Pad1) -> unconnected-(U98-Pad6)
- U99 pad 1: /Level Shifters/PAN5V.SCK_4_H2 -> /Level Shifters/PAN5V.MOSI_10
- U99 pad 3: /Level Shifters/PAN5V.MOSI_10 -> /Level Shifters/PAN5V.SCK_4_H2
- U99 pad 4: Net-(R284-Pad1) -> Net-(R283-Pad1)
- U99 pad 6: Net-(R283-Pad1) -> Net-(R284-Pad1)
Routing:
- net +5V: track 122.0 -> 319.4 mm, vias 64 -> 132
- net GND: track 142.0 -> 297.2 mm, vias 127 -> 259
- net Net-(U8-A1): track 0.00 -> 52.9 mm
- net Net-(U10-A1): track 0.00 -> 24.1 mm
- net /Panel Headers/MISO_01_P02: track 0.00 -> 4.13 mm
- net /Panel Headers/MISO_10_P11: track 0.00 -> 4.13 mm
- net /Panel Headers/MISO_04_P05: track 0.00 -> 4.13 mm
- net /Panel Headers/MISO_05_P06: track 0.00 -> 4.13 mm
- net /Panel Headers/MISO_02_P03: track 0.00 -> 4.13 mm
- net /Panel Headers/MISO_11_P12: track 0.00 -> 4.13 mm
- net /Panel Headers/MISO_08_P09: track 0.00 -> 4.13 mm
- net /Panel Headers/MISO_07_P08: track 0.00 -> 4.13 mm
- net /Panel Headers/MISO_09_P10: track 0.00 -> 4.13 mm
- net /Panel Headers/MISO_06_P07: track 0.00 -> 4.13 mm
- net /Panel Headers/MISO_03_P04: track 0.00 -> 4.13 mm
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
